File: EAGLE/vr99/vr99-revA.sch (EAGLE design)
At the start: 444 parts, among them Q0 2N7002, Q1 2N7002, Q2 2N7002, T2 AO3401A, T3 AO3401A, U1 STM32F411CEU7THERM, U2 74HC589A_DT, U3 74HC589A_DT, U4 74HC589A_DT, U5 TPS22995H-Q1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

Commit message: pre- GND routing save
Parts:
- removed D101, D102: DNP, jlcpcb_basic_parts:1N5819WS
- removed JKEY: MOLEX_0781710005, molex-pico-ezmate:MOLEX_0781710005
- added JDIP: MOLEX_0781710006, molex-pico-ezmate:MOLEX_0781710006
- D107: device SparkFun-LED:LED-BLUE0603 -> untitled:LED-REVERSE-MOUNT
- JTAG: value CORTEX_JTAG_DEBUG_PTH_NS -> TC2050IDC-NL; device SparkFun-Connectors:CORTEX_JTAG_DEBUG_PTH_NS -> ts_custom_nick_nacks:TC2050IDC-NL
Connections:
- removed net N$156: D102.A, JKEY.5
- removed net N$4: D101.A, JKEY.4
- new net N$10: JDIP.M
- net !RESET: now also U1A.!RST; no longer U1A.NRST
- net COL3: now also JDIP.3
- net COL4: now also JDIP.4; no longer D101.C
- net COL6: now also JDIP.5; no longer D102.C
- net COL7: now also JDIP.6
- net GND: now also JDIP.1, JTAG.GND@9, R12.4, R12.5, R13.1, R13.8, R14.4, R14.5, R15.1, R15.8; no longer JKEY.1, JKEY.M, JTAG.GNDDTCT
- net J_TCK: now also JTAG.SWDIO/TMS; no longer JTAG.SWDCLK/TCK
- net J_TDI: now also JTAG.TDI; no longer JTAG.NC/TDI
- net J_TMS: now also JTAG.SWCLK/TCK; no longer JTAG.SWDIO/TMS
- net RED10: now also R15.5; no longer R15.8
- net ROW3: no longer JKEY.2
- net ROW5: now also JDIP.2; no longer JKEY.3
- net VCC_2: now also JTAG.VTREF; no longer JTAG.VCC
- net XR10: now also R15.4; no longer R15.1
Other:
- note added: "(Optional) DIP_SWITCH_2"
- note added: "(Optional) DIP_SWITCH_3"
- note added: "(Optional) DIP_SWITCH_4"
- note added: "DIP SWITCH 1 DIP SWITCH 2 DIP SWITCH 3 DIP SWITCH 4"
- note added: "STATUS"
- note added: "STM32F411 MCU (Pins)"
- note removed: "STM32F411 MCU"
- moved on the sheet: R45, R46, R66, R70, Z101, Z102, Z103

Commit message: post GND-routing save
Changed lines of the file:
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@@
 Shift Registers</text>
 <text x="25.4" y="66.04" size="1.778" layer="91">BOOT1</text>
-<text x="27.178" y="52.578" size="1.778" layer="91">Status LED</text>
+<text x="26.162" y="54.102" size="1.778" layer="91">Status LED</text>
 <text x="218.44" y="104.14" size="1.778" layer="91">Shift/Reg Decoupling</text>
 <text x="187.96" y="165.1" size="1.778" layer="91">Shift/Reg / Col-scan Pulldowns</text>
@@
 and JST connector pinout need to
 be confirmed still.</text>
+<circle x="41.91" y="45.72" radius="4.572" width="0.1524" layer="104"/>
 </plain>
 <instances>
@@
 </instance>
 <instance part="D107" gate="G$1" x="40.64" y="45.72" smashed="yes">
-<attribute name="NAME" x="38.1" y="49.53" size="1.778" layer="95" font="vector"/>
-<attribute name="VALUE" x="38.1" y="43.18" size="1.778" layer="96" font="vector" align="top-left"/>
+<attribute name="NAME" x="39.37" y="50.8" size="1.778" layer="95" font="vector"/>
+<attribute name="VALUE" x="39.37" y="40.64" size="1.778" layer="96" font="vector" align="top-left"/>
 </instance>
 </instances>

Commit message: Beta 1
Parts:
- removed Q0: 2N7002, ts_custom_nick_nacks:2N7002-BSS138
- removed U_LED1, U_LED2: IS31FL3743B, ts_kb_mcu:IS31FL3743B
- added Q3: 2N7002, ts_custom_nick_nacks:2N7002-BSS138
- added U7, U8: TPS22995H-Q1, __untitled:TPS22995H-Q1
- U5, U6: value TPS22995H-Q1 -> IS31FL3743B; device __untitled:TPS22995H-Q1 -> ts_kb_mcu:IS31FL3743B
- renumbered EEP to EEPROM, T2 to Q4, T3 to Q5
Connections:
- removed net N$10: JDIP.M
- net GND: now also Q3.S, U5.EPAD, U5.GND, U5.PGND, U6.EPAD, U6.GND, U6.PGND, U7.G, U8.G; no longer Q0.S, U5.G, U6.G, U_LED1.EPAD, U_LED1.GND, U_LED1.PGND, U_LED2.EPAD, U_LED2.GND, U_LED2.PGND
- net LATCH: now also Q1.D; no longer Q0.D
- net LED1: now also U5.SW11; no longer U_LED1.SW11
- net LED10: now also U5.SW8; no longer U_LED1.SW8
- net LED11: now also U6.SW11; no longer U_LED2.SW11
- net LED12: now also U6.SW9; no longer U_LED2.SW9
- net LED13: now also U6.SW7; no longer U_LED2.SW7
- net LED14: now also U6.SW5; no longer U_LED2.SW5
- net LED15: now also U6.SW3; no longer U_LED2.SW3
- net LED16: now also U6.SW1; no longer U_LED2.SW1
- net LED17: now also U6.SW2; no longer U_LED2.SW2
- net LED18: now also U6.SW4; no longer U_LED2.SW4
- net LED19: now also U6.SW6; no longer U_LED2.SW6
- net LED1_CS: now also U5.CS; no longer U_LED1.CS
- net LED2: now also U5.SW9; no longer U_LED1.SW9
- net LED20: now also U6.SW8; no longer U_LED2.SW8
- net LED2_CS: now also U6.CS; no longer U_LED2.CS
- net LED3: now also U5.SW7; no longer U_LED1.SW7
- net LED4: now also U5.SW5; no longer U_LED1.SW5
- net LED5: now also U5.SW3; no longer U_LED1.SW3
- net LED6: now also U5.SW1; no longer U_LED1.SW1
- net LED7: now also U5.SW2; no longer U_LED1.SW2
- net LED8: now also U5.SW4; no longer U_LED1.SW4
- net LED9: now also U5.SW6; no longer U_LED1.SW6
- net LED_PWR_EN: now also U5.SDB, U6.SDB, U7.ON, U8.ON; no longer U5.ON, U6.ON, U_LED1.SDB, U_LED2.SDB
- net MATRIX_CS: now also Q1.G; no longer Q0.G
- net MISO: now also U5.MISO, U6.MISO; no longer U_LED1.MISO, U_LED2.MISO
- net MOSI: now also U5.MOSI, U6.MOSI; no longer U_LED1.MOSI, U_LED2.MOSI
- net N$1: now also U8.RT; no longer U6.RT
- net N$11: now also Q2.D; no longer Q1.D
- net N$12: now also Q2.G; no longer Q1.G
- net N$135: now also U7.RT; no longer U5.RT
- net N$136: now also U5.ISET; no longer U_LED1.ISET
- net N$151: now also U6.ISET; no longer U_LED2.ISET
- net N$7: now also Q3.D; no longer Q2.D
- net N$9: now also Q3.G; no longer Q2.G
- net SCK: now also U5.SCK, U6.SCK; no longer U_LED1.SCK, U_LED2.SCK
- net SYNC: now also U5.SYNC, U6.SYNC; no longer U_LED1.SYNC, U_LED2.SYNC
- net VCC_1: now also U7.BI, U7.IN, U8.BI, U8.IN; no longer U5.BI, U5.IN, U6.BI, U6.IN
- net VCC_LED_1: now also U5.PVCC, U5.VCC, U7.OUT; no longer U5.OUT, U_LED1.PVCC, U_LED1.VCC
- net VCC_LED_2: now also U6.PVCC, U6.VCC, U8.OUT; no longer U6.OUT, U_LED2.PVCC, U_LED2.VCC
- net XB1: now also U5.CS1; no longer U_LED1.CS1
- net XB10: now also U6.CS10; no longer U_LED2.CS10
- net XB11: now also U6.CS13; no longer U_LED2.CS13
- net XB12: now also U6.CS16; no longer U_LED2.CS16
- net XB2: now also U5.CS4; no longer U_LED1.CS4
- net XB3: now also U5.CS7; no longer U_LED1.CS7
- net XB4: now also U5.CS10; no longer U_LED1.CS10
- net XB5: now also U5.CS13; no longer U_LED1.CS13
- net XB6: now also U5.CS16; no longer U_LED1.CS16
- net XB7: now also U6.CS1; no longer U_LED2.CS1
- net XB8: now also U6.CS4; no longer U_LED2.CS4
- net XB9: now also U6.CS7; no longer U_LED2.CS7
- net XG1: now also U5.CS2; no longer U_LED1.CS2
- net XG10: now also U6.CS11; no longer U_LED2.CS11
- net XG11: now also U6.CS14; no longer U_LED2.CS14
- net XG12: now also U6.CS17; no longer U_LED2.CS17
- net XG2: now also U5.CS5; no longer U_LED1.CS5
- net XG3: now also U5.CS8; no longer U_LED1.CS8
- net XG4: now also U5.CS11; no longer U_LED1.CS11
- net XG5: now also U5.CS14; no longer U_LED1.CS14
- net XG6: now also U5.CS17; no longer U_LED1.CS17
- net XG7: now also U6.CS2; no longer U_LED2.CS2
- net XG8: now also U6.CS5; no longer U_LED2.CS5
- net XG9: now also U6.CS8; no longer U_LED2.CS8
- net XR1: now also U5.CS3; no longer U_LED1.CS3
- net XR10: now also U6.CS12; no longer U_LED2.CS12
- net XR11: now also U6.CS15; no longer U_LED2.CS15
- net XR12: now also U6.CS18; no longer U_LED2.CS18
- net XR2: now also U5.CS6; no longer U_LED1.CS6
- net XR3: now also U5.CS9; no longer U_LED1.CS9
- net XR4: now also U5.CS12; no longer U_LED1.CS12
- net XR5: now also U5.CS15; no longer U_LED1.CS15
- net XR6: now also U5.CS18; no longer U_LED1.CS18
- net XR7: now also U6.CS3; no longer U_LED2.CS3
- net XR8: now also U6.CS6; no longer U_LED2.CS6
- net XR9: now also U6.CS9; no longer U_LED2.CS9
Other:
- moved on the sheet: Q2

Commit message: Added "ground to boot" function
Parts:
- added Q6: BSH201, ts_custom_nick_nacks:BSH201
- added R28, R29: 100K, rcl:R-EU_R0603
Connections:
- removed net N$13: D100.A, R26.2, RST.2, S1.2
- new net !BOOT: Q6.G, R28.2, RST.2, S1.2
- new net BOOT: D100.A, Q6.D, R26.2, R29.2
- net GND: now also R29.1, RST.1, S1.1
- net VCC_2: now also Q6.S, R28.1; no longer RST.1, S1.1
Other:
- note added: "CHARLIE PIXEL DRIVERS"
- note added: "Hard Reset Ciruit"
- note added: "LED POWER SWITCHES"
- note added: "Optional Rotary Encoder"
- note added: "Partial (c) Gondolindrim Adapted from Figure 28 located at https://acheronproject.com/reset_article_1/reset_article_1/ (added BOOT inversion to allow GND-pull boot switch)"
- note added: "SKYLOONG Rotary Encoder 2 Positions - Only use 1 (A, B, & C are directly coupled)"
- note added: "nBOOT1 - Select Boot Area 1 = System memory 0 = Embedded SRAM"
- note removed: "(c) Gondolindrim - Figure 28 from https://acheronproject.com/reset_article_1/reset_article_1/"
- note removed: "Hard Reset"
- note removed: "LED POWER SWITCH"
- note removed: "SKYLONG Rotary Encoder 2 Positions - Only use 1"
- moved on the sheet: C25, C26, C27, C29, C30, D100, D107, JDIP, JI2C, JPWM, JSPI, JSPI@2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

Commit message: .
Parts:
- added C35, C36: 100nF, rcl:C-EUC0603
- added Q7: 2N7002, ts_custom_nick_nacks:2N7002-BSS138
- added R30, R31: 5.1K, rcl:R-EU_R0603
- added R32: 10K, rcl:R-EU_R0603
- added R33@1: 0R, rcl:R-EU_R0805W
- added R33@2, R34: 0R-DNP, rcl:R-EU_R0805W
- added U$7: ??, tecsmith_jlcpcb_ordering:JLC_ORDER_NUMBER_QRQR_8X8
- EEPROM: value M25C -> M25CDUAL; device ts_kb_mcu:M25C -> __tecsmith_kb_mcu:M25CDUAL
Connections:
- removed net N$110: D91.A, SW_SPC.P
- removed net PA8: JPWM.3, U1A.PA8
- removed net PB5: JPWM.4, U1A.PB5
- new net D91_A: D91.A, Q7.S, R34.2
- new net ENC_C: C31.1, R30.1, SW_F17G$1.A, U1A.PA8
- new net ENC_D: C32.1, R31.1, SW_F17G$1.B, U1A.PB5
- new net N$3: R33@1.2, R33@2.1, SW_SPC.S
- net AUX_CS: now also JPWM.4
- net AUX_DC: now also JPWM.3
- net ENC_A: now also C35.1; no longer C31.1, SW_F17G$1.A
- net ENC_B: now also C36.1; no longer C32.1, SW_F17G$1.B
- net GND: now also C35.2, C36.2, R32.2
- net ROW5: now also Q7.D, R33@2.2; no longer SW_SPC.S
- net VCC_2: now also R30.2, R31.2, R33@1.1
- net WKUP: now also Q7.G, R32.1, R34.1, SW_SPC.P
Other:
- note added: "2x SKYLOONG Rotary Encoder positions"
- note added: "5V Test Pad [0.1' PTH]"
- note added: "Debug Header [TC2050-IDC]"
- note added: "Monsgeek M2 Drop-In Mounting Holes (marked with Triangle) and JST connector pinout stil need to be confirmed."
- note added: "Optional / Aux SPI break-out [0.1' PTH]"
- note added: "Optional DIP Switch [Pico EzMate]"
- note added: "Optional I2C break-out [0.1' PTH]"
- note added: "Optional PWM break-out [0.1' PTH]"
- note added: "Space as Wake Up circuit {{ !! EXPERIMENTAL !! }}"
- note removed: "5V Test Pad"
- note removed: "Debug Header"
- note removed: "Monsgeek M2 Drop-In Mounting Holes (marked with Triangle) and JST connector pinout need to be confirmed still."
- note removed: "Optional / Aux SPI break-out"
- note removed: "Optional DIP Switch"
- note removed: "Optional I2C break-out"
- note removed: "Optional PWM break-out"
- note removed: "SKYLOONG Rotary Encoder 2 Positions - Only use 1 (A, B, & C are directly coupled)"
- moved on the sheet: C16, C17, C18, C19, C31, C32, H_SPC, JDIP, JI2C, JPWM, JSPI, JSPI@2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

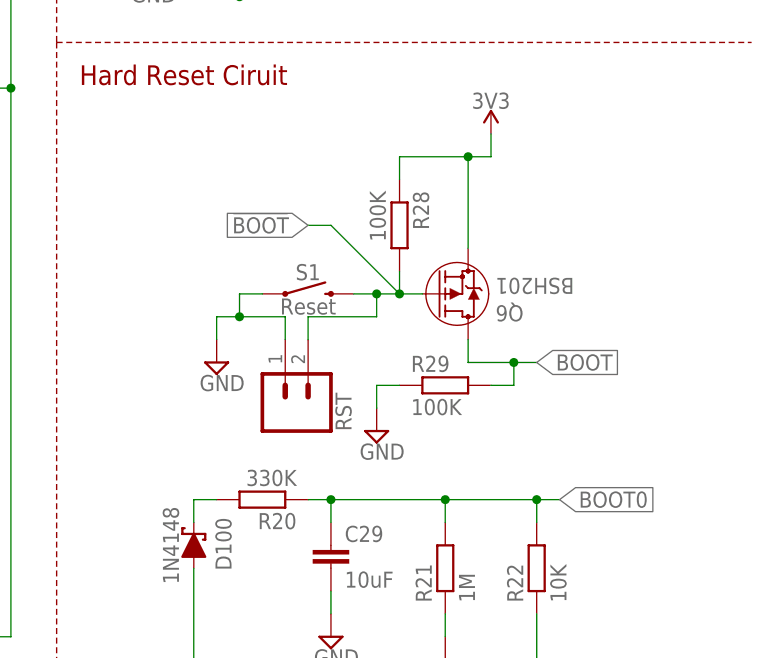
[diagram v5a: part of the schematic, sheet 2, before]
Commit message: confirmed m2 mounting points
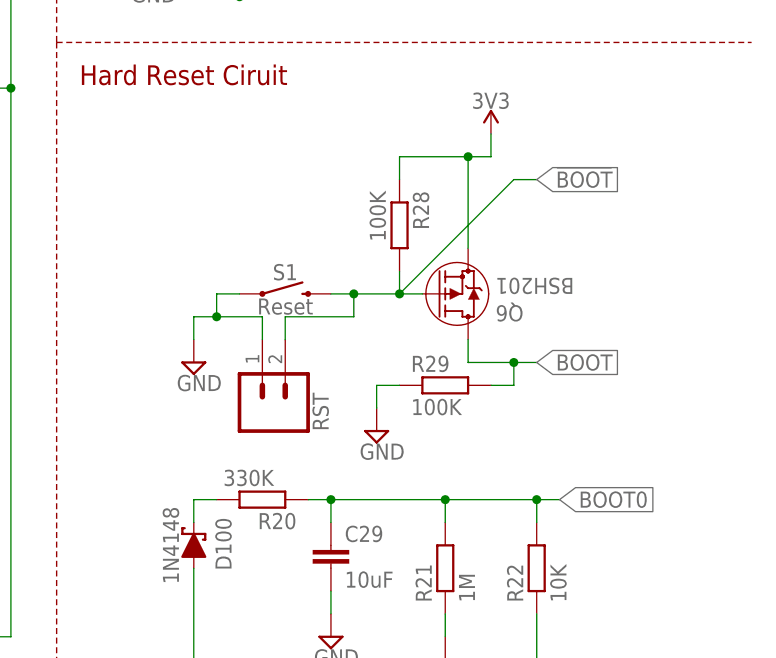
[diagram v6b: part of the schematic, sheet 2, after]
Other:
- moved on the sheet: RST, S1
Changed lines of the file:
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@@
 <attribute name="VALUE" x="317.5" y="18.034" size="1.778" layer="96" align="bottom-center"/>
 </instance>
-<instance part="S1" gate="G$1" x="330.2" y="127" smashed="yes">
-<attribute name="NAME" x="330.2" y="128.524" size="1.778" layer="95" font="vector" align="bottom-center"/>
-<attribute name="VALUE" x="330.2" y="126.492" size="1.778" layer="96" font="vector" align="top-center"/>
+<instance part="S1" gate="G$1" x="327.66" y="127" smashed="yes">
+<attribute name="NAME" x="327.66" y="128.524" size="1.778" layer="95" font="vector" align="bottom-center"/>
+<attribute name="VALUE" x="327.66" y="126.492" size="1.778" layer="96" font="vector" align="top-center"/>
 </instance>
 <instance part="C30" gate="G$1" x="353.06" y="48.26" smashed="yes" rot="R180">
@@
 <attribute name="VALUE" x="23.495" y="22.225" size="1.778" layer="96"/>
 </instance>
-<instance part="RST" gate="G$1" x="327.66" y="114.3" smashed="yes" rot="MR90">
-<attribute name="VALUE" x="322.834" y="111.76" size="1.778" layer="96" font="vector" rot="MR90"/>
-<attribute name="NAME" x="333.248" y="111.76" size="1.778" layer="95" font="vector" rot="MR90"/>
+<instance part="RST" gate="G$1" x="325.12" y="114.3" smashed="yes" rot="MR90">
+<attribute name="VALUE" x="320.294" y="111.76" size="1.778" layer="96" font="vector" rot="MR90"/>
+<attribute name="NAME" x="330.708" y="111.76" size="1.778" layer="95" font="vector" rot="MR90"/>
 </instance>
 <instance part="SUPPLY1" gate="G$1" x="325.12" y="238.76" smashed="yes">
@@
 <instance part="R20" gate="G$1" x="325.12" y="104.14" smashed="yes" rot="R180">
 <attribute name="NAME" x="328.93" y="102.6414" size="1.778" layer="95" rot="R180"/>
-<attribute name="VALUE" x="328.93" y="107.442" size="1.778" layer="96" rot="R180"/>
+<attribute name="VALUE" x="326.39" y="107.442" size="1.778" layer="96" rot="R180"/>
 </instance>
 <instance part="R21" gate="G$1" x="345.44" y="96.52" smashed="yes" rot="R90">
@@
 <attribute name="VALUE" x="351.028" y="128.778" size="1.778" layer="96" font="vector" ratio="10" rot="SMR180"/>
 </instance>
-<instance part="SUPPLY16" gate="GND" x="320.04" y="119.38" smashed="yes">
-<attribute name="VALUE" x="318.135" y="116.205" size="1.778" layer="96"/>
+<instance part="SUPPLY16" gate="GND" x="317.5" y="119.38" smashed="yes">
+<attribute name="VALUE" x="315.595" y="116.205" size="1.778" layer="96"/>
 </instance>
 <instance part="SUPPLY70" gate="G$1" x="350.52" y="144.78" smashed="yes">
@@
 <segment>
 <pinref part="S1" gate="G$1" pin="1"/>
-<wire x1="322.58" y1="127" x2="325.12" y2="127" width="0.1524" layer="91"/>
+<wire x1="320.04" y1="127" x2="322.58" y2="127" width="0.1524" layer="91"/>
 <pinref part="RST" gate="G$1" pin="1"/>
-<wire x1="327.66" y1="121.92" x2="327.66" y2="124.46" width="0.1524" layer="91"/>
-<wire x1="327.66" y1="124.46" x2="322.58" y2="124.46" width="0.1524" layer="91"/>
-<wire x1="322.58" y1="124.46" x2="322.58" y2="127" width="0.1524" layer="91"/>
-<wire x1="322.58" y1="124.46" x2="320.04" y2="124.46" width="0.1524" layer="91"/>
-<junction x="322.58" y="124.46"/>
+<wire x1="325.12" y1="121.92" x2="325.12" y2="124.46" width="0.1524" layer="91"/>
+<wire x1="325.12" y1="124.46" x2="320.04" y2="124.46" width="0.1524" layer="91"/>
+<wire x1="320.04" y1="124.46" x2="320.04" y2="127" width="0.1524" layer="91"/>
+<wire x1="320.04" y1="124.46" x2="317.5" y2="124.46" width="0.1524" layer="91"/>
+<junction x="320.04" y="124.46"/>
 <pinref part="SUPPLY16" gate="GND" pin="GND"/>
-<wire x1="320.04" y1="124.46" x2="320.04" y2="121.92" width="0.1524" layer="91"/>
+<wire x1="317.5" y1="124.46" x2="317.5" y2="121.92" width="0.1524" layer="91"/>
 </segment>
 <segment>
@@
 <segment>
 <pinref part="S1" gate="G$1" pin="2"/>
-<wire x1="335.28" y1="127" x2="337.82" y2="127" width="0.1524" layer="91"/>
-<wire x1="337.82" y1="124.46" x2="337.82" y2="127" width="0.1524" layer="91"/>
-<wire x1="330.2" y1="124.46" x2="337.82" y2="124.46" width="0.1524" layer="91"/>
+<wire x1="327.66" y1="124.46" x2="335.28" y2="124.46" width="0.1524" layer="91"/>
 <pinref part="RST" gate="G$1" pin="2"/>
-<wire x1="330.2" y1="121.92" x2="330.2" y2="124.46" width="0.1524" layer="91"/>
-<wire x1="337.82" y1="127" x2="340.36" y2="127" width="0.1524" layer="91"/>
-<junction x="337.82" y="127"/>
+<wire x1="327.66" y1="121.92" x2="327.66" y2="124.46" width="0.1524" layer="91"/>
+<wire x1="332.74" y1="127" x2="335.28" y2="127" width="0.1524" layer="91"/>
+<wire x1="335.28" y1="127" x2="340.36" y2="127" width="0.1524" layer="91"/>
 <wire x1="340.36" y1="127" x2="340.36" y2="129.54" width="0.1524" layer="91"/>
 <junction x="340.36" y="127"/>
 <pinref part="R28" gate="G$1" pin="2"/>
-<wire x1="340.36" y1="127" x2="332.74" y2="134.62" width="0.1524" layer="91"/>
-<wire x1="332.74" y1="134.62" x2="330.2" y2="134.62" width="0.1524" layer="91"/>
-<label x="330.2" y="134.62" size="1.778" layer="95" rot="R180" xref="yes"/>
+<wire x1="340.36" y1="127" x2="353.06" y2="139.7" width="0.1524" layer="91"/>
+<wire x1="353.06" y1="139.7" x2="355.6" y2="139.7" width="0.1524" layer="91"/>
+<label x="355.6" y="139.7" size="1.778" layer="95" xref="yes"/>
 <pinref part="Q6" gate="G$1" pin="G"/>
 <wire x1="342.9" y1="127" x2="340.36" y2="127" width="0.1524" layer="91"/>
-</segment>
-</net>
+<junction x="335.28" y="127"/>
+<wire x1="335.28" y1="127" x2="335.28" y2="124.46" width="0.1524" layer="91"/>
+</segment>
+</net>
